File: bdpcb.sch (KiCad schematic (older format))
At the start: 310 parts, among them J1 USB_C_Receptacle_USB2.0, J2 conn_female, K1 KEYSW, K10 KEYSW, K11 KEYSW, K12 KEYSW, K13 KEYSW, K14 KEYSW, K15 KEYSW, K16 KEYSW, K17 KEYSW, K18 KEYSW, K19 KEYSW, K2 KEYSW, K20 KEYSW, K21 KEYSW, K22 KEYSW, K23 KEYSW, K24 KEYSW, K25 KEYSW, K26 KEYSW, K27 KEYSW, K28 KEYSW, K29 KEYSW, K3 KEYSW, K30 KEYSW, K31 KEYSW, K32 KEYSW, K33 KEYSW, K34 KEYSW, K35 KEYSW, K36 KEYSW, K37 KEYSW, K38 KEYSW, K39 KEYSW, K4 KEYSW, K40 KEYSW, K41 KEYSW, K42 KEYSW, K43 KEYSW, K44 KEYSW, K45 KEYSW, K46 KEYSW, K47 KEYSW, K48 KEYSW, K49 KEYSW, K5 KEYSW, K50 KEYSW, K51 KEYSW, K52 KEYSW, K53 KEYSW, K54 KEYSW, K55 KEYSW, K56 KEYSW, K57 KEYSW, K58 KEYSW, K59 KEYSW, K6 KEYSW, K60 KEYSW, K61 KEYSW, K62 KEYSW, K63 KEYSW, K64 KEYSW, K65 KEYSW, K66 KEYSW, K67 KEYSW, K68 KEYSW, K69 KEYSW, K7 KEYSW, K70 KEYSW, K71 KEYSW, K72 KEYSW, K73 KEYSW, K74 KEYSW, K75 KEYSW, K76 KEYSW, K77 KEYSW, K78 KEYSW, K79 KEYSW, K8 KEYSW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

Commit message: removed mcu and BLE and power stuff
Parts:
- removed C1, C2: 22pF, symbol Device:C_Small
- removed C18, C19, C21: 10uF, symbol Device:C_Small
- removed C20, C3, C8, C9: 1uF, symbol Device:C_Small
- removed D84: red, symbol Device:LED_Small
- removed D85: blu, symbol Device:LED_Small
- removed D86: MBR1020VL, Diode_SMD:D_SOD-123F, symbol Diode:MBR1020VL
- removed D87: orng, symbol Device:LED_Small
- removed J2: conn_female, symbol Connector:Conn_01x16_Female
- removed R1, R19, R2: 10k, symbol Device:R
- removed R12, R15, R18: 100k, symbol Device:R
- removed R16: 1k, symbol Device:R
- removed R7, R8: 2.2k, symbol Device:R
- removed SW1: SW_PUSH, symbol HasuComponents:SW_PUSH
- removed U1: AT90USB1286-MU, Package_DFN_QFN:QFN-64-1EP_9x9mm_P0.5mm_EP7.5x7.5mm, symbol MCU_Microchip_AVR:AT90USB1286-MU
- removed U4: Adafruit 4076, 4076, symbol ecad:4076
- removed U5: SPX3819M5-L-3-3, Package_TO_SOT_SMD:SOT-23-5, symbol Regulator_Linear:SPX3819M5-L-3-3
- removed U6: MCP73831-2-OT, Package_TO_SOT_SMD:SOT-23-5, symbol Battery_Management:MCP73831-2-OT
- removed X1: JSTPH_2, symbol ai03Symbols:JSTPH_2
- removed Y1: 16MHz, symbol Device:Crystal_GND24_Small
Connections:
- net labels added: D+
- net labels removed: +BATT, 4_SWDIO_RST, 7_BLE_IRQ, 8_BLE_CS, DFU, DIV, FCTRYRST, MISO, MOSI, PB0, PB5, PB6, PB7, PD0, PD1, PD2, PE0, PE1, PE3, PE4, PE5, PE7, PF1, PF2, SCK, SWCLK
- wire segments 1427 -> 1338
- no-connect marks 34 -> 11
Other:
- note added: "nts: dont forget\nto calculate\ndifferential\nimpedance"
- note removed: "AREF of 3V3 means\nvoltage divider needed\nto read battery level"
- note removed: "BLE package"
- note removed: "CONNECTED"
- note removed: "I figure I'll just have some\nthrough hole pinout for the\nunused mcu gpio pins in\ncase i ever want to use em"
- note removed: "I know I'm gonna mess something up\non my first PCB prototype ever so\nI'll probably split this into two boards\n(one for matrices, one for the brains)\nconnected by a ribbon cable or two"
- note removed: "LDO linear regulator"
- note removed: "LiPo charger"
- note removed: "MODE"
- note removed: "Power Stuff"
- note removed: "TODO: add slide switch\nor button to enable pin"
- note removed: "battery analog pin here\nbecause i think PF0 is ADC\nchannel 0 on at90usb128"
- note removed: "battery\nconnector"
- note removed: "charging\nindicator"
- note removed: "i can still use ADC\npins for whatever,\nright?"
- note removed: "is a 10uF and 1uF\ndecoupling enough\nfor this setup?"
- note removed: "is this bad for\nbattery life?"
- note removed: "just chose these pins randomly\nit doesn't matter, right?\ni can just specify in firmware, right?"
- note removed: "need to have\nsomething to dfu\npin for flashing"
- note removed: "nts: dont forget to calculate differential impedance"
- note removed: "same pin as\n32u4 Feather"
- note removed: "same pins as\n32u4 Feather"
- note removed: "should i divide by some\nvalue other than 2 to get\n4.2V to 3.3V?"
- note removed: "voltage divider\nfor reading\nbattery level"
- moved on the sheet: D1, D10, D11, D12, D13, D14, D15, D16, D17, D18, D19, D2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

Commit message: IO expander not integrated yet
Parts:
- removed R3, R4: 22, symbol Device:R
- added U?: MCP23017_SO, Package_SO:SOIC-28W_7.5x17.9mm_P1.27mm, symbol Interface_Expansion:MCP23017_SO
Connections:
- net D+: now also J1.A6 (D+), J1.A7 (D-), J1.B6 (D+), J1.B7 (D-)
- net INTB: now also U?.19 (INTB)
- net SCL: now also U?.12 (SCK)
- net SDA: now also U?.13 (SDA)
- net VBUS: now also F1.2; no longer F1.1
- net col0: now also U?.1 (GPB0)
- net col1: now also U?.2 (GPB1)
- net col10: now also U?.23 (GPA2)
- net col11: now also U?.24 (GPA3)
- net col12: now also U?.25 (GPA4)
- net col13: now also U?.26 (GPA5)
- net col14: now also U?.27 (GPA6)
- net col2: now also U?.3 (GPB2)
- net col3: now also U?.4 (GPB3)
- net col4: now also U?.5 (GPB4)
- net col5: now also U?.6 (GPB5)
- net col6: now also U?.7 (GPB6)
- net col7: now also U?.8 (GPB7)
- net col8: now also U?.21 (GPA0)
- net col9: now also U?.22 (GPA1)
- net at J1.A4 (VBUS), J1.A9 (VBUS), J1.B4 (VBUS)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: now also F1.1; no longer F1.2
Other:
- note removed: "not the most "efficient" matrix, i know, but I've got extra GPIO anyways"
- moved on the sheet: C10, C11, C12, C13, C14, C15, C16, C17, C22, C23, C24, C25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

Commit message: scott's suggestions and new LED symbol/footprints
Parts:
- removed F1: 500mA, symbol Device:Polyfuse_Small
- removed J1: USB_C_Receptacle_USB2.0, symbol Connector:USB_C_Receptacle_USB2.0
- removed L1, L10, L11, L12, L13, L14, L15, L16, L17, L18, L19, L2, L20, L21, L22, L23, L24, L25, L26, L27, L28, L29, L3, L30, L31, L32, L33, L34, L35, L36, L37, L38, L39, L4, L40, L41, L42, L43, L44, L45, L46, L47, L48, L49, L5, L50, L51, L52, L53, L54, L55, L56, L57, L58, L59, L6, L60, L61, L62, L63, L64, L65, L66, L67, L68, L69, L7, L70, L71, L72, L73, L74, L75, L76, L77, L78, L79, L8, L80, L81, L82, L83, L9: LED_BRAG, symbol Device:LED_BRAG
- removed R10, R11: 1k, symbol Device:R
- removed R5, R6: 5.1k, symbol Device:R
- removed R9: 100k, symbol Device:R
- added C1: 0.1uF, Capacitor_SMD:C_0805_2012Metric, symbol Device:C_Small
- added JP1, JP2, JP3, JP5, JP6, JP8, JP9: 13_bridge, Jumper:SolderJumper-3_P1.3mm_Bridged12_RoundedPad1.0x1.5mm, symbol Jumper:SolderJumper_3_Bridged12
- added JP4, JP7: 12_bridge, Jumper:SolderJumper-2_P1.3mm_Bridged_RoundedPad1.0x1.5mm, symbol Jumper:SolderJumper_2_Bridged
- added L1, L10, L11, L12, L13, L14, L15, L16, L17, L18, L19, L2, L20, L21, L22, L23, L24, L25, L26, L27, L28, L29, L3, L30, L31, L32, L33, L34, L35, L36, L37, L38, L39, L4, L40, L41, L42, L43, L44, L45, L46, L47, L48, L49, L5, L50, L51, L52, L53, L54, L55, L56, L57, L58, L59, L6, L60, L61, L62, L63, L64, L65, L66, L67, L68, L69, L7, L70, L71, L72, L73, L74, L75, L76, L77, L78, L79, L8, L80, L81, L82, L83, L9: QBLP677R-RGB, QB_RGB_LED_footprint:RGB-REVERSE_MOUNT, symbol QB_RGB_LED:QBLP677R-RGB
- added R1, R2: 2.2k, Resistor_SMD:R_0805_2012Metric, symbol Device:R
- added R3: 100k, Resistor_SMD:R_0805_2012Metric, symbol Device:R
- added SW1: SW_SPDT, Button_Switch_SMD:SW_SPDT_CK-JS102011SAQN, symbol Switch:SW_SPDT
- added TP1, TP4, TP5: TestPoint, TestPoint:TestPoint_Pad_D2.5mm, symbol Connector:TestPoint
- added TP2, TP3: TestPoint, TestPoint:TestPoint_Plated_Hole_D2.0mm, symbol Connector:TestPoint
- added U1: Adafruit_2829, featherFootprint:ADAFRUIT_2829, symbol feather:Adafruit_2829
- C10: renamed from C22; footprint (none) -> Capacitor_SMD:C_0805_2012Metric
- C11: renamed from C23; footprint (none) -> Capacitor_SMD:C_0805_2012Metric
- C12: renamed from C24; footprint (none) -> Capacitor_SMD:C_0805_2012Metric
- C13: renamed from C25; footprint (none) -> Capacitor_SMD:C_0805_2012Metric
- C14: renamed from C26; footprint (none) -> Capacitor_SMD:C_0805_2012Metric
- C15: renamed from C27; footprint (none) -> Capacitor_SMD:C_0805_2012Metric
- C16: renamed from C28; footprint (none) -> Capacitor_SMD:C_0805_2012Metric
- C17: renamed from C29; footprint (none) -> Capacitor_SMD:C_0805_2012Metric
- C2: renamed from C10; footprint (none) -> Capacitor_SMD:C_0805_2012Metric
- C3: renamed from C11; footprint (none) -> Capacitor_SMD:C_0805_2012Metric
- C4: renamed from C12; footprint (none) -> Capacitor_SMD:C_0805_2012Metric
- C5: renamed from C13; footprint (none) -> Capacitor_SMD:C_0805_2012Metric
- C6: renamed from C14; footprint (none) -> Capacitor_SMD:C_0805_2012Metric
- C7: renamed from C15; footprint (none) -> Capacitor_SMD:C_0805_2012Metric
- C8: renamed from C16; footprint (none) -> Capacitor_SMD:C_0805_2012Metric
- C9: renamed from C17; footprint (none) -> Capacitor_SMD:C_0805_2012Metric
- D1, D10, D11, D12, D13, D14, D15, D16, D17, D18, D19, D2, D20, D21, D22, D23, D24, D25, D26, D27, D28, D29, D3, D30, D31, D32, D33, D34, D35, D36, D37, D38, D39, D4, D40, D41, D42, D43, D44, D45, D46, D47, D48, D49, D5, D50, D51, D52, D53, D54, D55, D56, D57, D58, D59, D6, D60, D61, D62, D63, D64, D65, D66, D67, D68, D69, D7, D70, D71, D72, D73, D74, D75, D76, D77, D78, D79, D8, D80, D81, D82, D83, D9: footprint (none) -> Diode_SMD:D_SOD-123
- K1, K10, K11, K12, K13, K14, K15, K16, K17, K18, K19, K2, K20, K21, K22, K23, K24, K25, K26, K27, K28, K29, K3, K30, K32, K33, K34, K35, K36, K37, K38, K39, K4, K40, K41, K42, K43, K46, K47, K48, K49, K5, K50, K51, K52, K53, K54, K55, K56, K59, K6, K60, K61, K62, K63, K64, K65, K66, K67, K68, K69, K7, K70, K71, K76, K78, K79, K8, K80, K81, K82, K83, K9: footprint (none) -> ai03Footprints:MXOnly-1U-NoLED
- K31, K44: footprint (none) -> ai03Footprints:MXOnly-1.5U-NoLED
- K45: footprint (none) -> ai03Footprints:MXOnly-1.75U-NoLED
- K57: footprint (none) -> ai03Footprints:MXOnly-2.25U-NoLED
- K58, K75, K77: footprint (none) -> ai03Footprints:MXOnly-2U-NoLED
- K72, K73, K74: footprint (none) -> ai03Footprints:MXOnly-1.25U-NoLED
- R4: renamed from R13; footprint (none) -> Resistor_SMD:R_0805_2012Metric
- R5: renamed from R14; footprint (none) -> Resistor_SMD:R_0805_2012Metric
- R6: renamed from R17; footprint (none) -> Resistor_SMD:R_0805_2012Metric
- R7: renamed from R20; footprint (none) -> Resistor_SMD:R_0805_2012Metric
- gave numbers to parts that had none: 1
- renumbered U2 to U3, U3 to U4
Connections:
- net +3V3: now also U2.18 (~RESET~), U2.9 (VDD), C1.1, JP1.3 (B), JP2.3 (B), JP3.3 (B), JP4.1 (A), JP5.3 (B), JP6.3 (B), JP7.1 (A), JP8.3 (B), JP9.1 (A), R1.2, R2.2, R3.2, U1.14 (3V3); no longer C10.1, C11.1, C12.1, C13.1, C14.1, C15.1, C16.1, C2.1, C3.1, C4.1, C5.1, C6.1, C7.1, C8.1, U3.20 (PVCC), U3.29 (PVCC), U3.37 (AVCC), U3.38 (DVCC), U4.20 (PVCC), U4.29 (PVCC), U4.37 (AVCC), U4.38 (DVCC), U4.43 (ADDR1)
- net GND: now also U2.10 (VSS), C1.2, JP1.1 (A), JP2.1 (A), JP3.1 (A), JP5.1 (A), JP6.1 (A), JP8.1 (A), JP9.3 (B), SW1.2 (B), TP2.1, U1.15 (GND); no longer U3.43 (ADDR1), U3.44 (ADDR2), U4.44 (ADDR2)
- net IICRST: now also U1.29 (PB5)
- net INTB: now also R3.1, U1.27 (PD7); no longer U2.19 (INTB)
- net LA_1: now also L1.COMMON_ANODE, L16.COMMON_ANODE, L31.COMMON_ANODE, TP4.1
- net LA_10: now also L10.COMMON_ANODE, L25.COMMON_ANODE, L40.COMMON_ANODE
- net LA_11: now also L11.COMMON_ANODE, L26.COMMON_ANODE, L41.COMMON_ANODE
- net LA_12: now also L12.COMMON_ANODE, L27.COMMON_ANODE, L42.COMMON_ANODE
- net LA_13: now also L13.COMMON_ANODE, L28.COMMON_ANODE, L43.COMMON_ANODE
- net LA_14: now also L14.COMMON_ANODE, L29.COMMON_ANODE, L44.COMMON_ANODE
- net LA_15: now also L15.COMMON_ANODE, L30.COMMON_ANODE
- net LA_2: now also L17.COMMON_ANODE, L2.COMMON_ANODE, L32.COMMON_ANODE
- net LA_3: now also L18.COMMON_ANODE, L3.COMMON_ANODE, L33.COMMON_ANODE
- net LA_4: now also L19.COMMON_ANODE, L34.COMMON_ANODE, L4.COMMON_ANODE
- net LA_5: now also L20.COMMON_ANODE, L35.COMMON_ANODE, L5.COMMON_ANODE
- net LA_6: now also L21.COMMON_ANODE, L36.COMMON_ANODE, L6.COMMON_ANODE
- net LA_7: now also L22.COMMON_ANODE, L37.COMMON_ANODE, L7.COMMON_ANODE
- net LA_8: now also L23.COMMON_ANODE, L38.COMMON_ANODE, L8.COMMON_ANODE
- net LA_9: now also L24.COMMON_ANODE, L39.COMMON_ANODE, L9.COMMON_ANODE
- net LA_A: now also L1.2, L10.2, L11.2, L12.2, L13.2, L14.2, L15.2, L2.2, L3.2, L4.2, L5.2, L6.2, L7.2, L8.2, L9.2
- net LA_B: now also L1.3, L10.3, L11.3, L12.3, L13.3, L14.3, L15.3, L2.3, L3.3, L4.3, L5.3, L6.3, L7.3, L8.3, L9.3
- net LA_C: now also L1.1, L10.1, L11.1, L12.1, L13.1, L14.1, L15.1, L2.1, L3.1, L4.1, L5.1, L6.1, L7.1, L8.1, L9.1
- net LA_D: now also L16.2, L17.2, L18.2, L19.2, L20.2, L21.2, L22.2, L23.2, L24.2, L25.2, L26.2, L27.2, L28.2, L29.2, L30.2
- net LA_E: now also L16.3, L17.3, L18.3, L19.3, L20.3, L21.3, L22.3, L23.3, L24.3, L25.3, L26.3, L27.3, L28.3, L29.3, L30.3
- net LA_F: now also L16.1, L17.1, L18.1, L19.1, L20.1, L21.1, L22.1, L23.1, L24.1, L25.1, L26.1, L27.1, L28.1, L29.1, L30.1
- net LA_G: now also L31.2, L32.2, L33.2, L34.2, L35.2, L36.2, L37.2, L38.2, L39.2, L40.2, L41.2, L42.2, L43.2, L44.2
- net LA_H: now also L31.3, L32.3, L33.3, L34.3, L35.3, L36.3, L37.3, L38.3, L39.3, L40.3, L41.3, L42.3, L43.3, L44.3
- net LA_I: now also L31.1, L32.1, L33.1, L34.1, L35.1, L36.1, L37.1, L38.1, L39.1, L40.1, L41.1, L42.1, L43.1, L44.1
- net LB_1: now also L45.COMMON_ANODE, L58.COMMON_ANODE, L72.COMMON_ANODE, TP5.1
- net LB_10: now also L54.COMMON_ANODE, L67.COMMON_ANODE, L79.COMMON_ANODE
- net LB_11: now also L55.COMMON_ANODE, L68.COMMON_ANODE, L80.COMMON_ANODE
- net LB_12: now also L56.COMMON_ANODE, L69.COMMON_ANODE, L81.COMMON_ANODE
- net LB_13: now also L70.COMMON_ANODE, L82.COMMON_ANODE
- net LB_14: now also L57.COMMON_ANODE
- net LB_15: now also L71.COMMON_ANODE, L83.COMMON_ANODE
- net LB_2: now also L46.COMMON_ANODE, L59.COMMON_ANODE, L73.COMMON_ANODE
- net LB_3: now also L47.COMMON_ANODE, L60.COMMON_ANODE, L74.COMMON_ANODE
- net LB_4: now also L48.COMMON_ANODE, L61.COMMON_ANODE, L75.COMMON_ANODE
- net LB_5: now also L49.COMMON_ANODE, L62.COMMON_ANODE
- net LB_6: now also L50.COMMON_ANODE, L63.COMMON_ANODE, L76.COMMON_ANODE
- net LB_7: now also L51.COMMON_ANODE, L64.COMMON_ANODE
- net LB_8: now also L52.COMMON_ANODE, L65.COMMON_ANODE, L77.COMMON_ANODE
- net LB_9: now also L53.COMMON_ANODE, L66.COMMON_ANODE, L78.COMMON_ANODE
- net LB_A: now also L45.2, L46.2, L47.2, L48.2, L49.2, L50.2, L51.2, L52.2, L53.2, L54.2, L55.2, L56.2, L57.2
- net LB_B: now also L45.3, L46.3, L47.3, L48.3, L49.3, L50.3, L51.3, L52.3, L53.3, L54.3, L55.3, L56.3, L57.3
- net LB_C: now also L45.1, L46.1, L47.1, L48.1, L49.1, L50.1, L51.1, L52.1, L53.1, L54.1, L55.1, L56.1, L57.1
- net LB_D: now also L58.2, L59.2, L60.2, L61.2, L62.2, L63.2, L64.2, L65.2, L66.2, L67.2, L68.2, L69.2, L70.2, L71.2
- net LB_E: now also L58.3, L59.3, L60.3, L61.3, L62.3, L63.3, L64.3, L65.3, L66.3, L67.3, L68.3, L69.3, L70.3, L71.3
- net LB_F: now also L58.1, L59.1, L60.1, L61.1, L62.1, L63.1, L64.1, L65.1, L66.1, L67.1, L68.1, L69.1, L70.1, L71.1
- net LB_G: now also L72.2, L73.2, L74.2, L75.2, L76.2, L77.2, L78.2, L79.2, L80.2, L81.2, L82.2, L83.2
- net LB_H: now also L72.3, L73.3, L74.3, L75.3, L76.3, L77.3, L78.3, L79.3, L80.3, L81.3, L82.3, L83.3
- net LB_I: now also L72.1, L73.1, L74.1, L75.1, L76.1, L77.1, L78.1, L79.1, L80.1, L81.1, L82.1, L83.1
- net SCL: now also R2.1, U1.18 (PD0/SCL)
- net SDA: now also R1.1, U1.19 (PD1/SDA)
- net SDB: now also U1.31 (PC6)
- net col0: now also U2.21 (GPA0), TP1.1; no longer U2.1 (GPB0)
- net col1: now also U2.22 (GPA1); no longer U2.2 (GPB1)
- net col10: now also U2.5 (GPB4); no longer U2.23 (GPA2)
- net col11: now also U2.4 (GPB3); no longer U2.24 (GPA3)
- net col12: now also U2.3 (GPB2); no longer U2.25 (GPA4)
- net col13: now also U2.2 (GPB1); no longer U2.26 (GPA5)
- net col14: now also U2.1 (GPB0); no longer U2.27 (GPA6)
- net col2: now also U2.23 (GPA2); no longer U2.3 (GPB2)
- net col3: now also U2.24 (GPA3); no longer U2.4 (GPB3)
- net col4: now also U2.25 (GPA4); no longer U2.5 (GPB4)
- net col5: now also U2.26 (GPA5); no longer U2.6 (GPB5)
- net col6: now also U2.27 (GPA6); no longer U2.7 (GPB6)
- net col7: now also U2.28 (GPA7); no longer U2.8 (GPB7)
- net col8: now also U2.7 (GPB6); no longer U2.21 (GPA0)
- net col9: now also U2.6 (GPB5); no longer U2.22 (GPA1)
- net row0: now also U1.41 (PF0)
- net row1: now also U1.40 (PF1)
- net row2: now also U1.39 (PF4)
- net row3: now also U1.38 (PF5)
- net row4: now also U1.37 (PF6)
- net row5: now also U1.36 (PF7)
- net at U2.15 (A0): now also JP3.2 (C)
- net at U2.16 (A1): now also JP2.2 (C)
- net at U2.17 (A2): now also JP1.2 (C)
- new net: SW1.1 (A), TP3.1, U1.3 (En)
- new net: C2.1, C3.1, C4.1, C5.1, C6.1, C7.1, C8.1, JP4.2 (B), U3.20 (PVCC), U3.29 (PVCC), U3.37 (AVCC), U3.38 (DVCC)
- new net: JP6.2 (C), U3.43 (ADDR1)
- new net: JP5.2 (C), U3.44 (ADDR2)
- new net: C10.1, C11.1, C12.1, C13.1, C14.1, C15.1, C16.1, JP7.2 (B), U4.20 (PVCC), U4.29 (PVCC), U4.37 (AVCC), U4.38 (DVCC)
- new net: JP9.2 (C), U4.43 (ADDR1)
- new net: JP8.2 (C), U4.44 (ADDR2)
- no-connect marks 11 -> 27
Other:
- note added: "(reverse-mount SMD common-anode RGB)"
- note added: "2.2k i2c pullups\nmay prefer 5.7k?"
- note added: "AREF uses\ninternal 3V3\nby default"
- note added: "Adafruit 32u4 Feather Bluefruit LE dev board"
- note added: "SPI pins\nused by\nBluefruit"
- note added: "addr 0100000X\nX is R/W bit"
- note added: "i2c I/O expander"
- note added: "i2c LED matrix driver"
- note added: "power\nslide\nswitch"
- note removed: "nts: dont forget\nto calculate\ndifferential\nimpedance"
- note removed: "planning on using reverse mount 5050 or 6028 packages or smth"
- moved on the sheet: C10, C11, C12, C13, C14, C15, C16, C17, C2, C3, C4, C5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

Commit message: starting pcb
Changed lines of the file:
@@
 Text Notes 9400 6425 0    50   ~ 0
 (reverse-mount SMD common-anode RGB)
+Text Notes 1500 11625 0    50   ~ 0
+nts: use tantalum\ncapacitor here\nto avoid noise
 $EndSCHEMATC

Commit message: fixed feather footprint pinout to match symbol
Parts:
- K75, K77: footprint ai03Footprints:MXOnly-2U-NoLED -> ai03Footprints:MXOnly-2U-ReversedStabilizers-NoLED
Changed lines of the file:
@@
 F 0 "K77" H 10325 5425 60  0000 C CNN
 F 1 "KEYSW" H 10325 5325 60  0001 C CNN
-F 2 "ai03Footprints:MXOnly-2U-NoLED" H 10325 5425 60  0001 C CNN
+F 2 "ai03Footprints:MXOnly-2U-ReversedStabilizers-NoLED" H 10325 5425 60  0001 C CNN
 F 3 "" H 10325 5425 60  0000 C CNN
 	1    10325 5425
@@
 F 0 "K75" H 7325 5425 60  0000 C CNN
 F 1 "KEYSW" H 7325 5325 60  0001 C CNN
-F 2 "ai03Footprints:MXOnly-2U-NoLED" H 7325 5425 60  0001 C CNN
+F 2 "ai03Footprints:MXOnly-2U-ReversedStabilizers-NoLED" H 7325 5425 60  0001 C CNN
 F 3 "" H 7325 5425 60  0000 C CNN
 	1    7325 5425

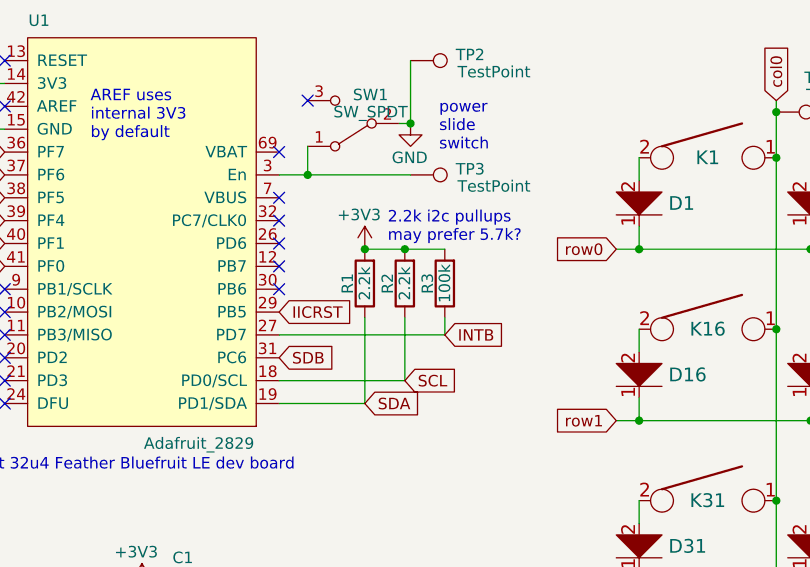
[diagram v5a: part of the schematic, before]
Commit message: 4.7k i2c pullups and laying row tracks
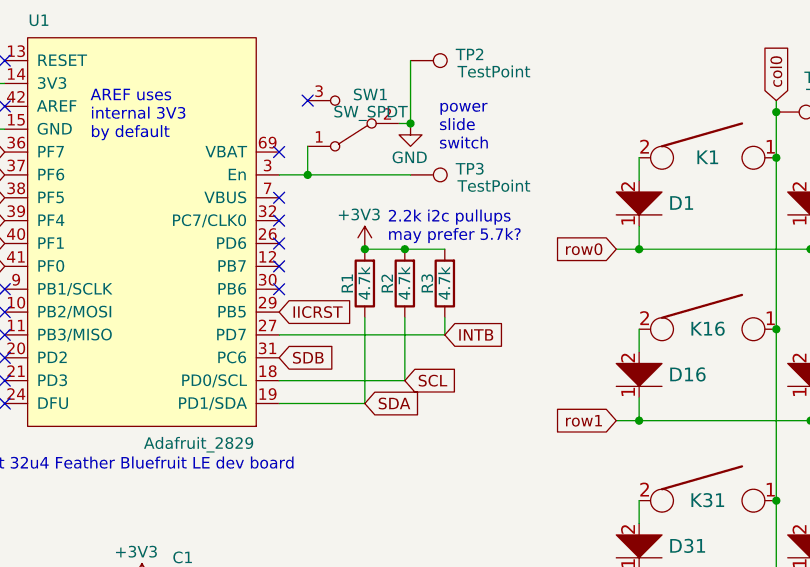
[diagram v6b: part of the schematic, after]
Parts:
- R1, R2: value 2.2k -> 4.7k
- R3: value 100k -> 4.7k
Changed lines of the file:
@@
 P 3575 2225
 F 0 "R1" V 3650 2225 50  0000 C CNN
-F 1 "2.2k" V 3575 2225 50  0000 C CNN
+F 1 "4.7k" V 3575 2225 50  0000 C CNN
 F 2 "Resistor_SMD:R_0805_2012Metric" V 3505 2225 50  0001 C CNN
 F 3 "~" H 3575 2225 50  0001 C CNN
@@
 P 3750 2225
 F 0 "R2" V 3825 2225 50  0000 C CNN
-F 1 "2.2k" V 3750 2225 50  0000 C CNN
+F 1 "4.7k" V 3750 2225 50  0000 C CNN
 F 2 "Resistor_SMD:R_0805_2012Metric" V 3680 2225 50  0001 C CNN
 F 3 "~" H 3750 2225 50  0001 C CNN
@@
 Wire Wire Line
 	3925 2375 3925 2450
-$Comp
-L Device:R R3
-U 1 1 69CB0D2D
-P 3925 2225
-F 0 "R3" V 4000 2225 50  0000 C CNN
-F 1 "100k" V 3925 2225 50  0000 C CNN
-F 2 "Resistor_SMD:R_0805_2012Metric" V 3855 2225 50  0001 C CNN
-F 3 "~" H 3925 2225 50  0001 C CNN
-	1    3925 2225
-	-1   0    0    1
-$EndComp
 Text GLabel 3925 2450 2    50   Input ~ 0
 INTB
@@
 Text Notes 1500 11625 0    50   ~ 0
 nts: use tantalum\ncapacitor here\nto avoid noise
+$Comp
+L Device:R R3
+U 1 1 69CB0D2D
+P 3925 2225
+F 0 "R3" V 4000 2225 50  0000 C CNN
+F 1 "4.7k" V 3925 2225 50  0000 C CNN
+F 2 "Resistor_SMD:R_0805_2012Metric" V 3855 2225 50  0001 C CNN
+F 3 "~" H 3925 2225 50  0001 C CNN
+	1    3925 2225
+	-1   0    0    1
+$EndComp
 $EndSCHEMATC

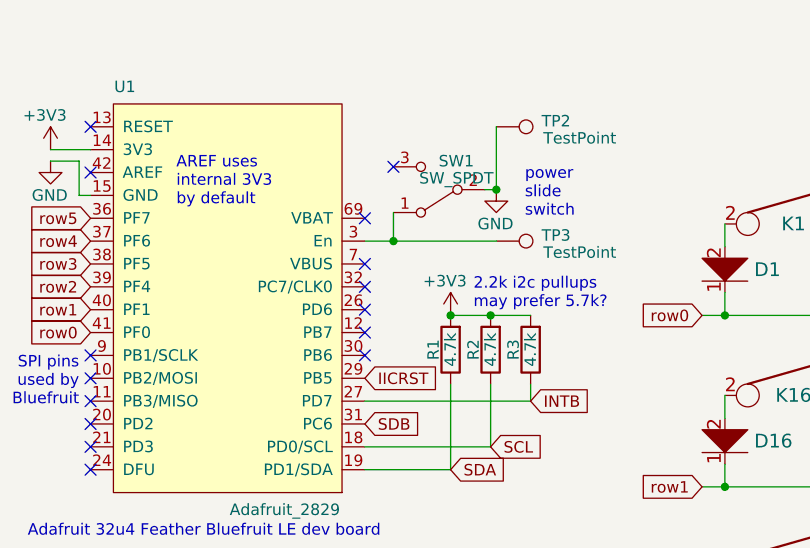
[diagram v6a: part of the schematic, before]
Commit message: figured out how to change power track width
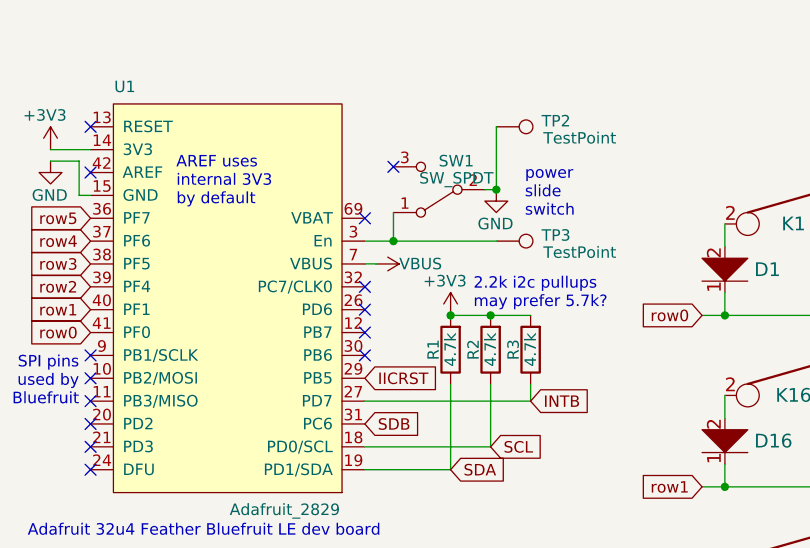
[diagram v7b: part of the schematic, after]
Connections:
- net VBUS: now reaches U1.7 (VBUS)
- no-connect marks 27 -> 26
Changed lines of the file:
@@
 NoConn ~ 2000 2550
 NoConn ~ 3200 1650
-NoConn ~ 3200 1850
 NoConn ~ 3200 1950
 NoConn ~ 3200 2050
@@
 	-1   0    0    1
 $EndComp
+$Comp
+L power:VBUS #PWR?
+U 1 1 6204CA71
+P 3250 1850
+F 0 "#PWR?" H 3250 1700 50  0001 C CNN
+F 1 "VBUS" V 3250 1950 50  0000 L CNN
+F 2 "" H 3250 1850 50  0001 C CNN
+F 3 "" H 3250 1850 50  0001 C CNN
+	1    3250 1850
+	0    1    1    0
+$EndComp
+Wire Wire Line
+	3200 1850 3250 1850
 $EndSCHEMATC

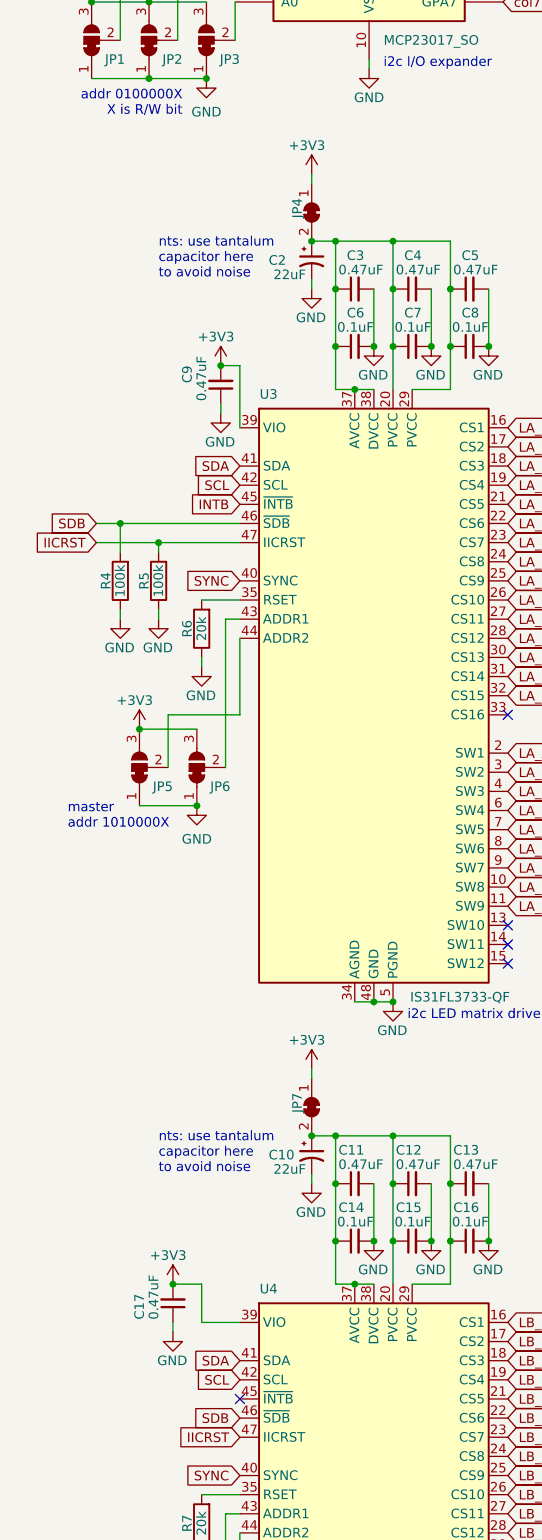
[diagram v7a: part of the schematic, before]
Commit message: added VBUS/3V3 bridges for driver power
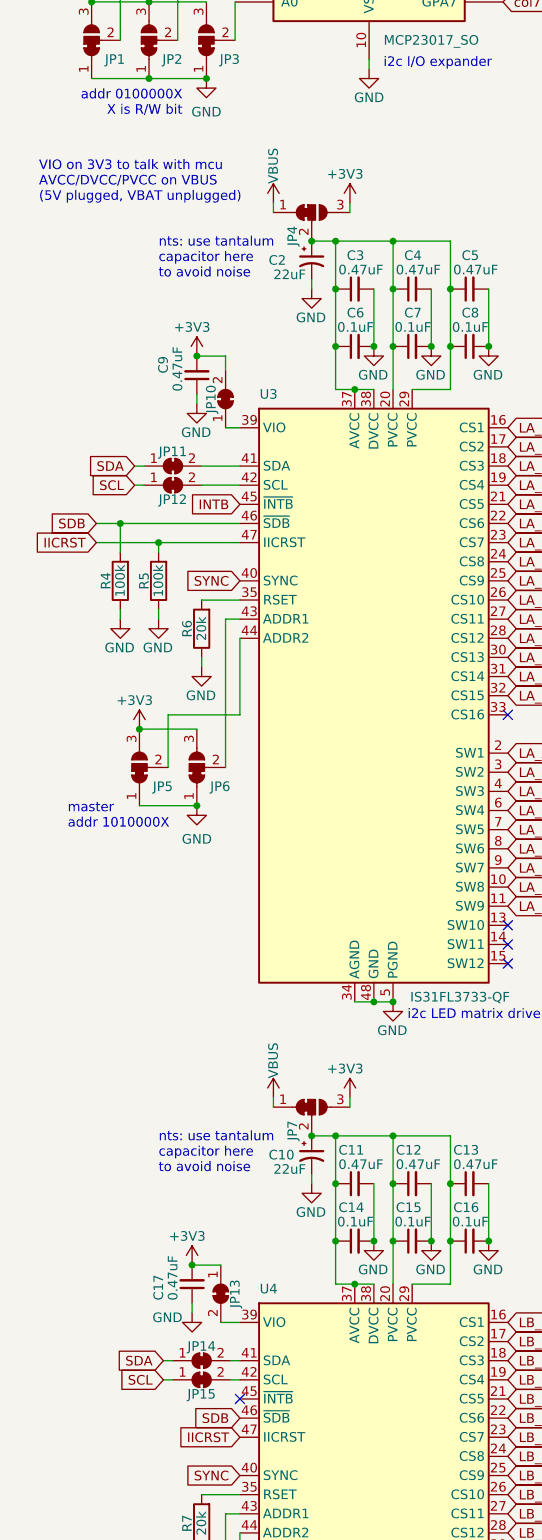
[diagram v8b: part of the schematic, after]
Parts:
- removed JP4, JP7: 12_bridge, Jumper:SolderJumper-2_P1.3mm_Bridged_RoundedPad1.0x1.5mm, symbol Jumper:SolderJumper_2_Bridged
- added JP10, JP11, JP12, JP13, JP14, JP15: SolderJumper_2_Bridged, Jumper:SolderJumper-2_P1.3mm_Bridged_RoundedPad1.0x1.5mm, symbol Jumper:SolderJumper_2_Bridged
- added JP4, JP7: 13_bridge, Jumper:SolderJumper-3_P1.3mm_Bridged12_RoundedPad1.0x1.5mm, symbol Jumper:SolderJumper_3_Bridged12
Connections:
- net +3V3: now also JP10.2 (B), JP13.1 (A), JP4.3 (B), JP7.3 (B); no longer U3.39 (VIO), U4.39 (VIO)
- net SCL: now also JP12.1 (A), JP15.1 (A); no longer U3.42 (SCL), U4.42 (SCL)
- net SDA: now also JP11.1 (A), JP14.1 (A); no longer U3.41 (SDA), U4.41 (SDA)
- net VBUS: now also JP4.1 (A), JP7.1 (A)
- net at C2.1, C3.1, C4.1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: now also JP4.2 (C)
- net at C10.1, C11.1, C12.1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: now also JP7.2 (C)
- new net: JP14.2 (B), U4.41 (SDA)
- new net: JP15.2 (B), U4.42 (SCL)
- new net: JP11.2 (B), U3.41 (SDA)
- new net: JP12.2 (B), U3.42 (SCL)
- new net: JP10.1 (A), U3.39 (VIO)
- new net: JP13.2 (B), U4.39 (VIO)
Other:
- note added: "VIO on 3V3 to talk with mcu\nAVCC/DVCC/PVCC on VBUS\n(5V plugged, VBAT unplugged)"
- moved on the sheet: C17, C9
